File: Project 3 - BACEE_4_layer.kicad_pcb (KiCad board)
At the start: 2 copper layers, 40.4 x 29.7 mm, 17 parts, among them J1 Digital pins, J2 Serial, J3 ICSP, J4 I2C, U1 DS1337S, U2 24LC1025, U3 24LC1025, U4 ATMEGA328P-AU, Y1 Crystal 32 MHz, Y2 Crystal 16 MHz

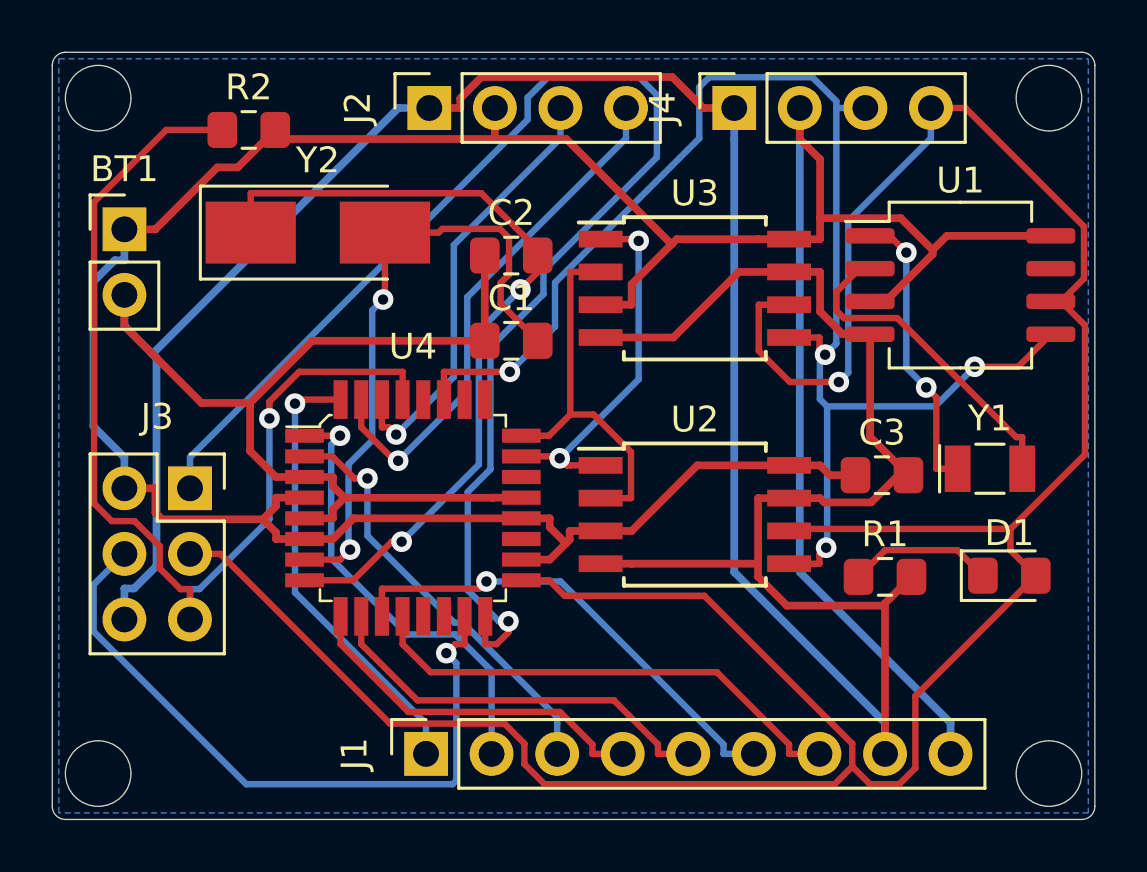
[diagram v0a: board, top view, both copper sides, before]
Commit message: Created copper filled area for 2-layer board and 4-layer board.
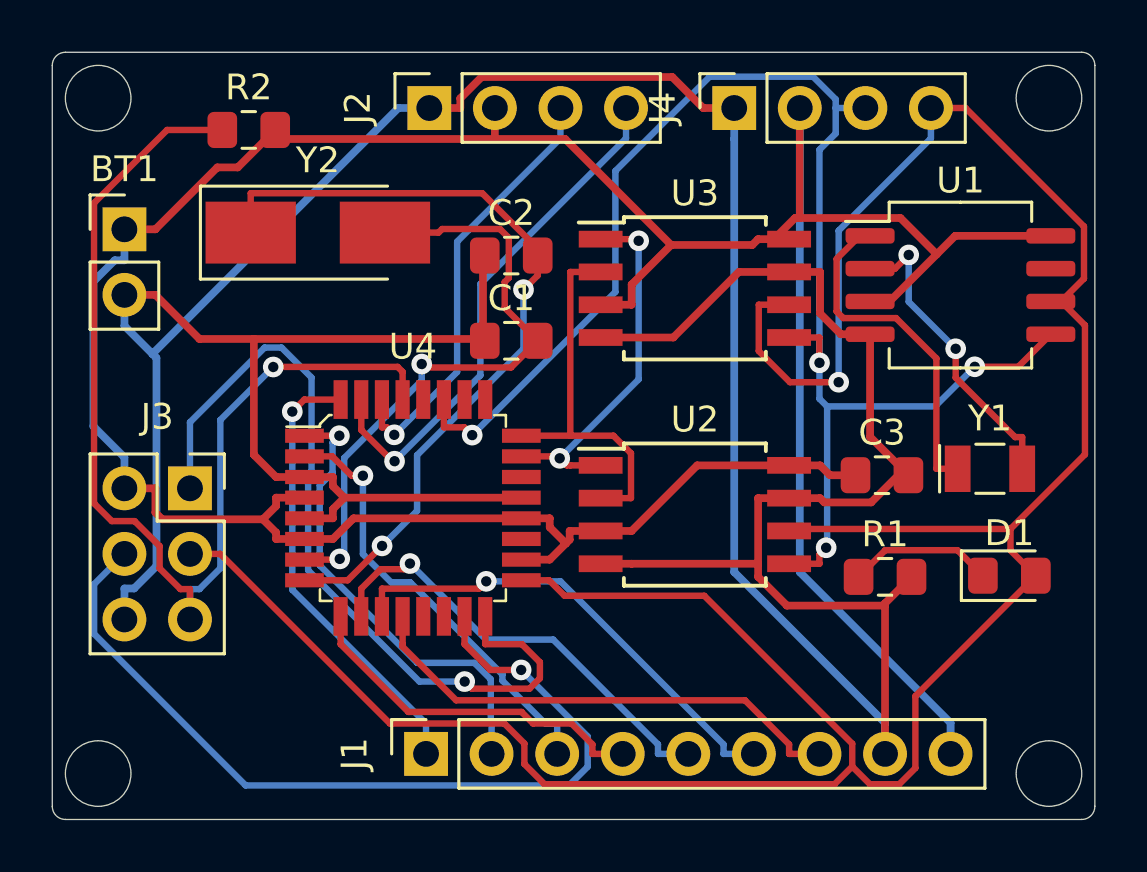
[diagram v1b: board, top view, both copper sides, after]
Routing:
- net /MISO: track 53.1 -> 31.6 mm
- net /MOSI: track 27.1 -> 33.9 mm
- net Net-(U1-Pad1): track 11.4 -> 13.4 mm, vias 2 -> 0
- net /SDA: track 56.0 -> 58.0 mm
- net /D6: track 15.7 -> 17.4 mm, vias 0 -> 1
- net Net-(U1-Pad2): track 12.9 -> 12.0 mm, vias 0 -> 2
- net /RESET: track 41.2 -> 42.0 mm
- net /D3: track 17.5 -> 18.0 mm
- added copper zone on In2.Cu, net GNDPWR
- removed copper zone on B.Cu, net GNDPWR
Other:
- copper layers 2 -> 4
